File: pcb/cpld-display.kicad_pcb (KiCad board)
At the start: 2 copper layers, 59 x 38 mm, 75 parts, among them J1 USB_C_Receptacle_USB2.0_16P, J2 Conn_02x03_Odd_Even, SW1 SW_Push, SW2 SW_Push, SW3 SW_Push, U1 AMS1117-3.3, U2 AMS1117-1.8, U3 XC2C64A-7QFG48C, U4 ULN2003A, U5 ULN2003A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

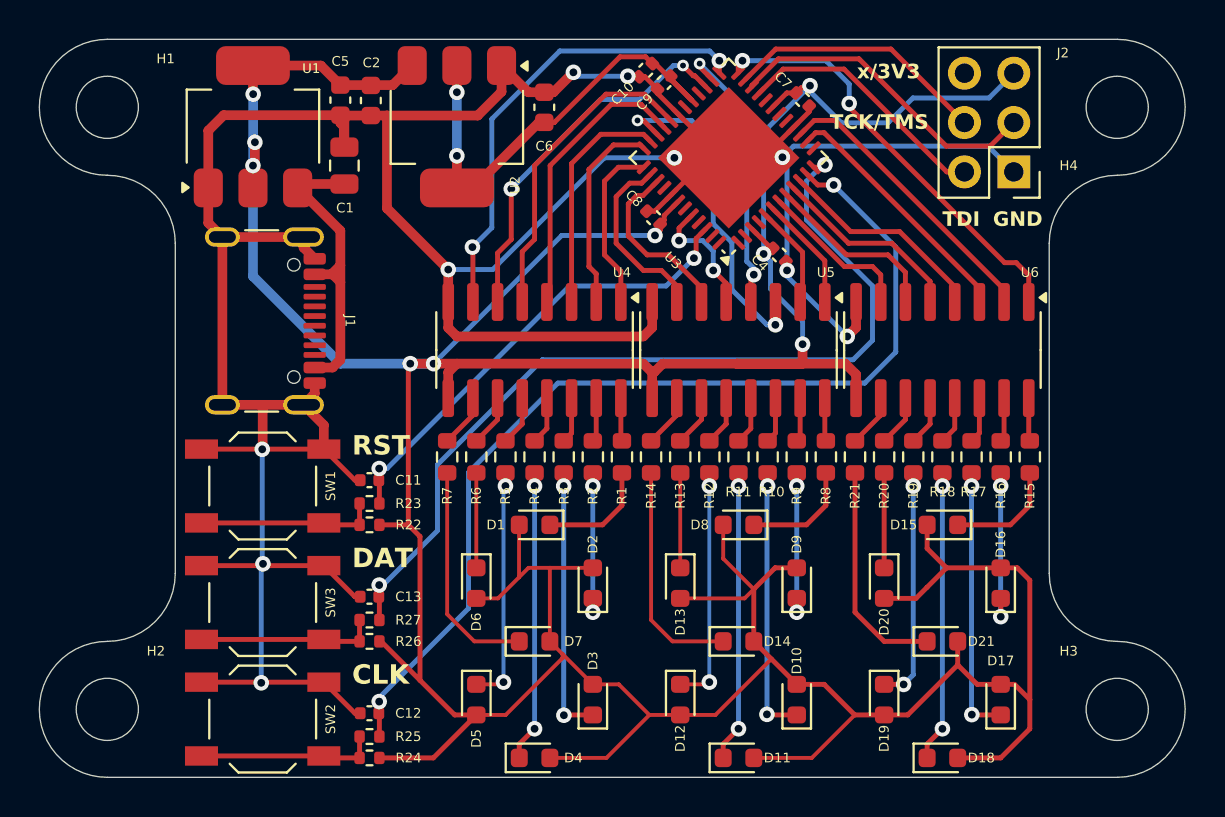
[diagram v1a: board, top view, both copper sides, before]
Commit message: Fix jtag tdo pin
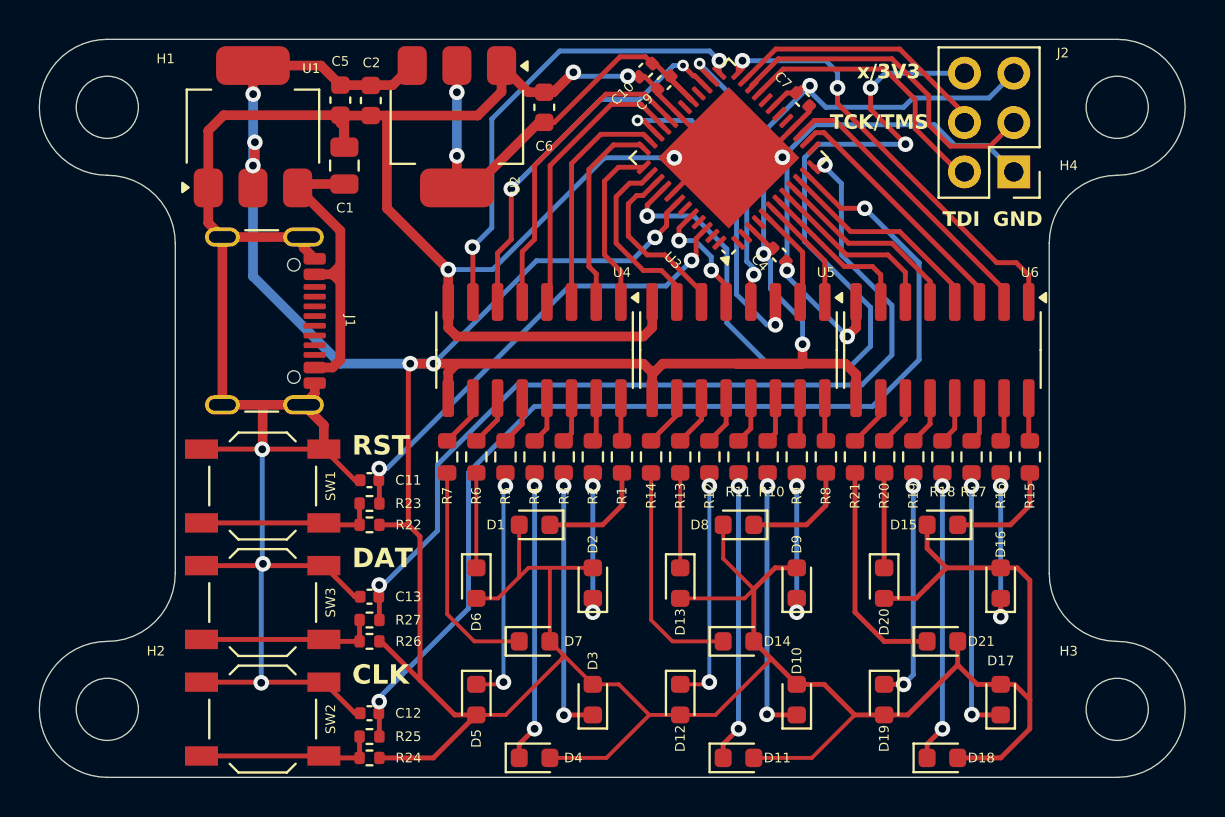
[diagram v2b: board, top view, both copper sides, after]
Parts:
- removed C8: 100n, Capacitor_SMD:C_0402_1005Metric
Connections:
- J2 pad 6: unconnected-(J2-Pin_6-Pad6) -> /TDO
- U3 pad 40: unconnected-(U3-TDO-Pad40) -> /TDO
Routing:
- net /TDO: track 0.00 -> 44.5 mm, vias 0 -> 3
- net /CLK: track 51.6 -> 53.8 mm
- net /DATA: track 46.0 -> 47.1 mm
- net /TMS: track 16.5 -> 17.4 mm
- net /TDI: track 13.3 -> 14.2 mm
- net GND: track 180.9 -> 180.2 mm
- net +3V3: track 245.6 -> 245.0 mm
